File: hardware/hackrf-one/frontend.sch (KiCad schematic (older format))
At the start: 144 parts, among them J10 GND_CLIP, J2 RF-SHIELD-FRAME, J3 RF-SHIELD-COVER, J4 MOUNTING_HOLE, J5 MOUNTING_HOLE, J6 MOUNTING_HOLE, J7 MOUNTING_HOLE, J8 MOUNTING_HOLE, J9 MOUNTING_HOLE, P13 GPO1, P17 GPO6, P19 GPO3, P21 REF_IN, P27 MIXER_SDATA, P31 MIXER_SCLK, P32 MIXER_ENX, P33 MIXER_RESETX, P34 MIX_BYPASS, P35 !MIX_BYPASS, P4 ANTENNA, P42 TX, P43 RX, P44 HP, P45 LP, P46 TX_MIX_BP, P47 RX_MIX_BP, P48 TX_AMP, P49 RX_AMP, P50 AMP_BYPASS, P51 !TX_AMP_PWR, P52 !RX_AMP_PWR, P6 GPO4, P7 GPO2, Q1 MOSFET_P, Q2 MOSFET_P, Q4 MOSFET_P, T1 MIX_IN_BALUN, T2 MIX_OUT_BALUN, U1 SKY13350, U10 SKY13350, U11 SKY13350, U12 SKY13317, U13 MGA-81563, U14 SKY13317, U2 SKY13350, U25 MGA-81563, U3 RX_LOWPASS_FILTER, U4 RFFC5072, U5 SKY13350, U6 SKY13350, U7 SKY13350, U8 RX_HIGHPASS_FILTER, U9 SKY13317

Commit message: Corrected libraries (to use gsg-kicad-lib) and added SMP1330 protection
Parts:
- added C117: 100nF, hackrf:GSG-0402, symbol hackrf-one-rescue:C
- added D20, D21: SMP1330-005LF, SOT23-DD, symbol gsg-symbols:SMP1330-005LF
- added R38, R39: 10k, hackrf:GSG-0402, symbol hackrf-one-rescue:R
- C1, C10, C11, C12, C13, C14, C15, C16, C160, C161, C162, C163, C166, C17, C171, C18, C19, C2, C20, C21, C22, C23, C24, C25, C26, C27, C28, C29, C3, C30, C31, C32, C33, C34, C35, C36, C37, C38, C39, C4, C40, C41, C42, C43, C44, C45, C46, C47, C48, C49, C5, C50, C51, C52, C53, C54, C55, C56, C57, C58, C59, C6, C60, C61, C62, C63, C64, C65, C66, C67, C7, C70, C8, C9: symbol C -> hackrf-one-rescue:C
- D1: symbol GSG-DIODE-TVS-BI -> hackrf-one-rescue:GSG-DIODE-TVS-BI
- J10, J4, J5, J6, J7, J8, J9, P13, P17, P19, P21, P27, P31, P32, P33, P34, P35, P42, P43, P44, P45, P46, P47, P48, P49, P50, P51, P52, P6, P7: symbol CONN_1 -> hackrf-one-rescue:CONN_1
- J2: symbol RF-SHIELD-FRAME -> hackrf-one-rescue:RF-SHIELD-FRAME
- J3: symbol RF-SHIELD-COVER -> hackrf-one-rescue:RF-SHIELD-COVER
- L1, L12, L13, L2, L3, L4, L5: symbol INDUCTOR -> hackrf-one-rescue:INDUCTOR
- P4: symbol GSG-RF-CONN -> hackrf-one-rescue:GSG-RF-CONN
- Q1, Q2, Q4: symbol MOSFET_P -> hackrf-one-rescue:MOSFET_P
- R1, R2, R24, R29, R3, R36, R4, R5, R6: symbol R -> hackrf-one-rescue:R
- T1, T2: symbol BALUN-B0310J50100AHF -> hackrf-one-rescue:BALUN-B0310J50100AHF
- U1, U10, U11, U2, U5, U6, U7: symbol SKY13350 -> hackrf-one-rescue:SKY13350
- U12, U14, U9: symbol SKY13317 -> hackrf-one-rescue:SKY13317
- U13, U25: symbol MGA-81563 -> hackrf-one-rescue:MGA-81563
- U3: symbol FIL-LP0603 -> hackrf-one-rescue:FIL-LP0603
- U4: symbol RFFC5072 -> hackrf-one-rescue:RFFC5072
- U8: symbol FIL-DEA -> hackrf-one-rescue:FIL-DEA
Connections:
- wire segments 367 -> 452

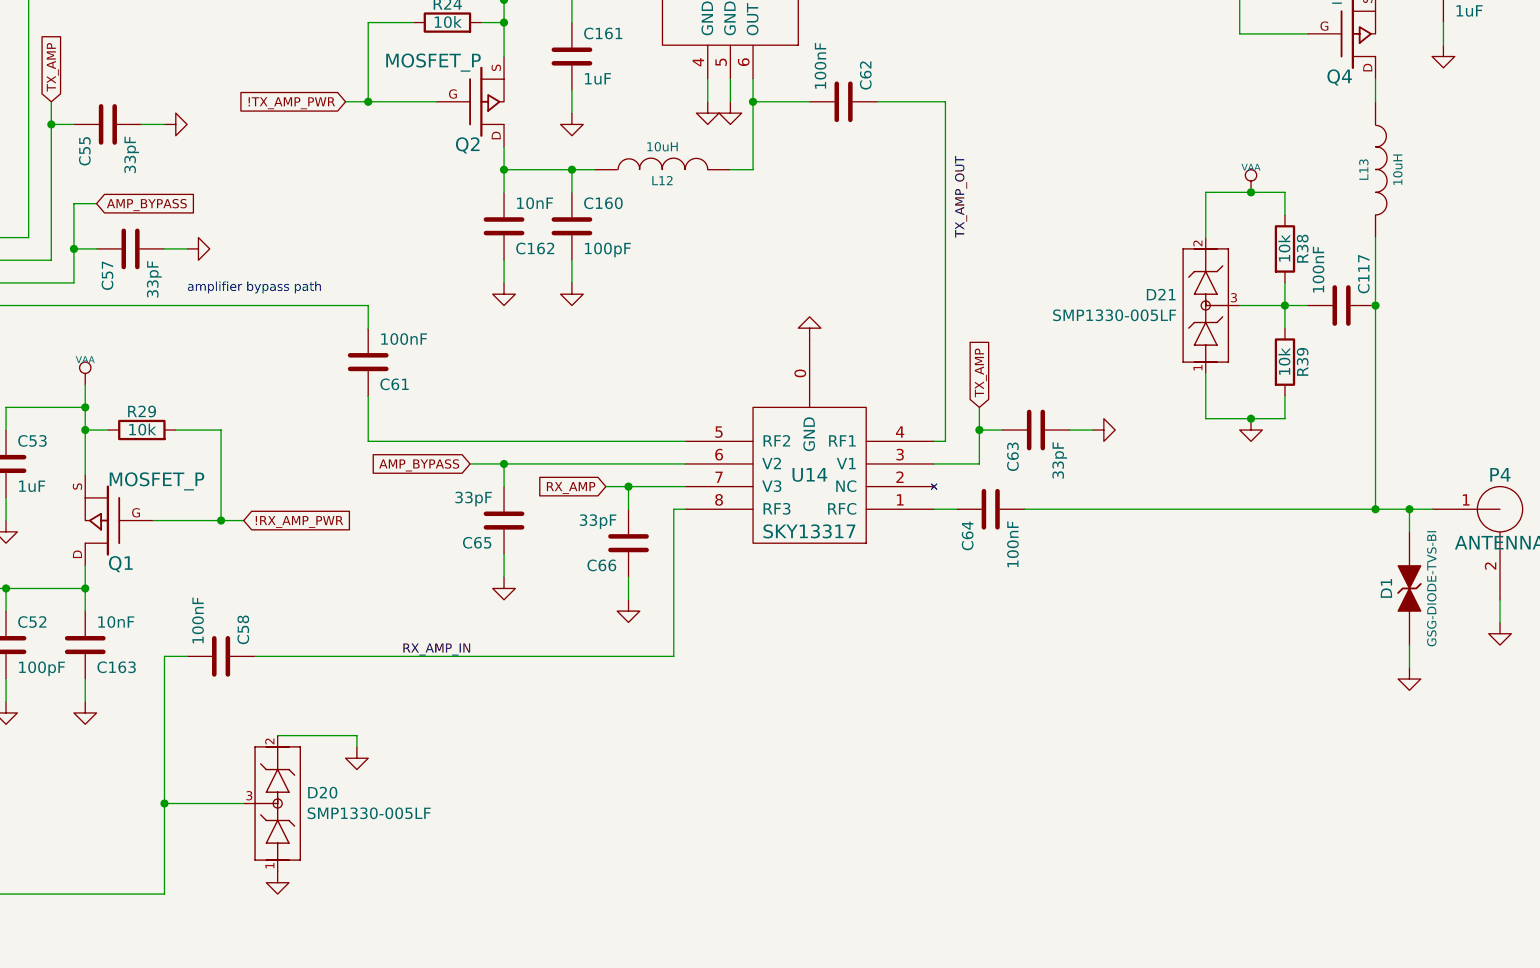
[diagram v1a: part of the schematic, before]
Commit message: Improved RF layout by passing signals through protection devices instead of using stubs
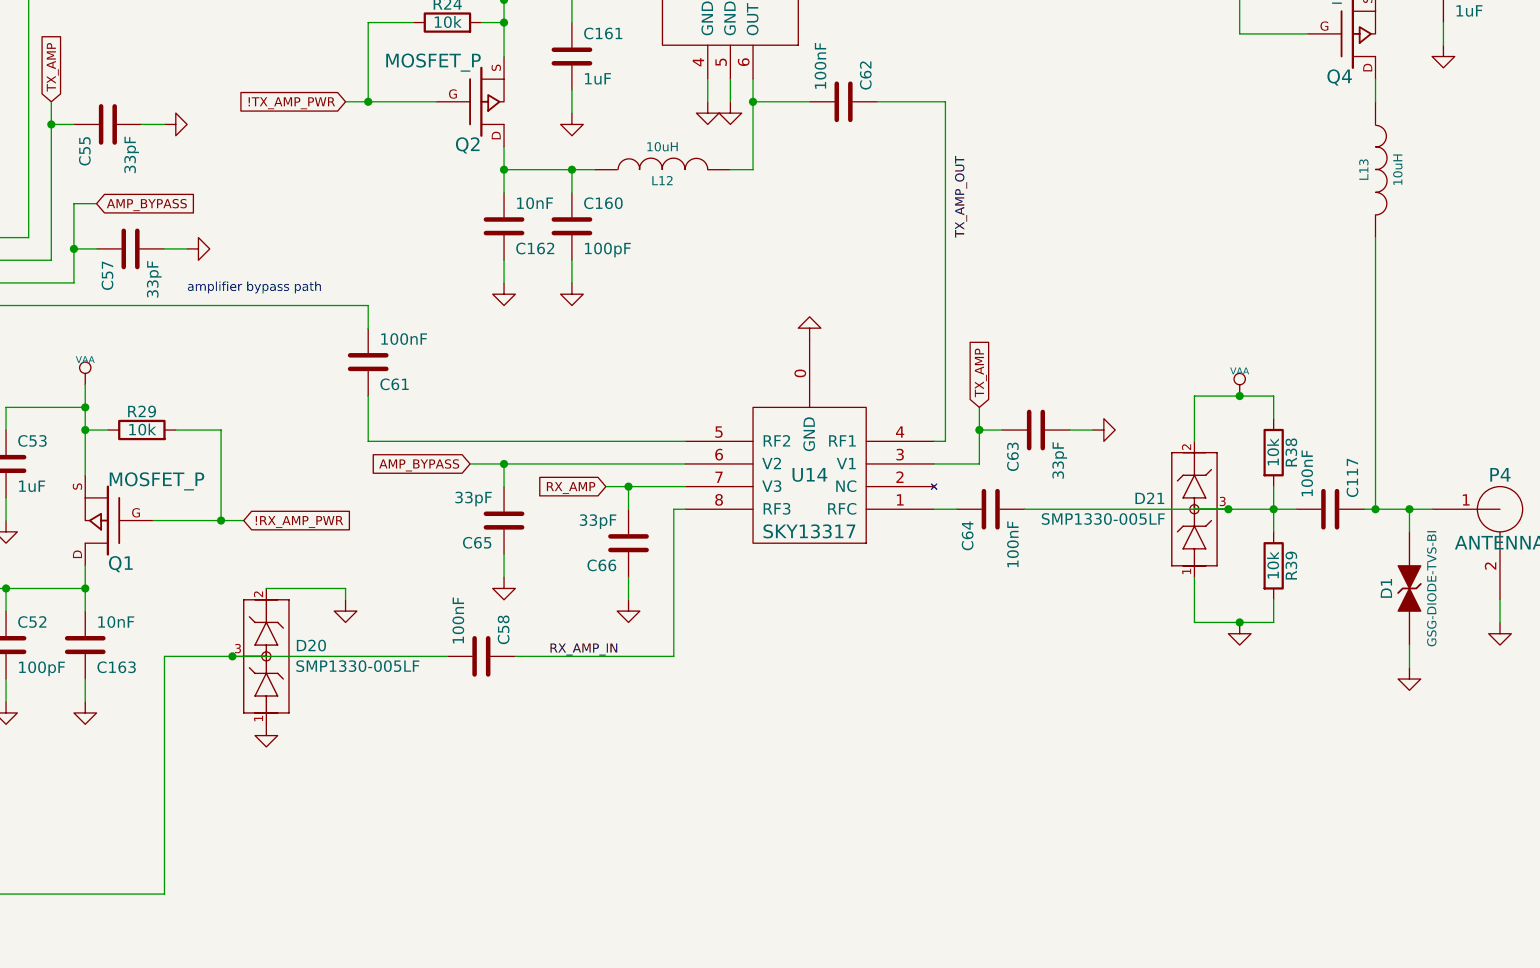
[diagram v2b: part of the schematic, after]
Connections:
- net at C117.1, D1.2 (K), L13.2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: no longer C64.2
- net at C117.2, D21.3, R38.2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: now also C64.2
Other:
- moved on the sheet: C117, C58, D20, D21, R38, R39
